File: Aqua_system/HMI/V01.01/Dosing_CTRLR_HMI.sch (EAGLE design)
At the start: 62 parts, among them IC1 74LS47N, Q1 BC817, Q2 BC817, Q3 BC817, Q4 BC817, X1 MICROMATCH-16

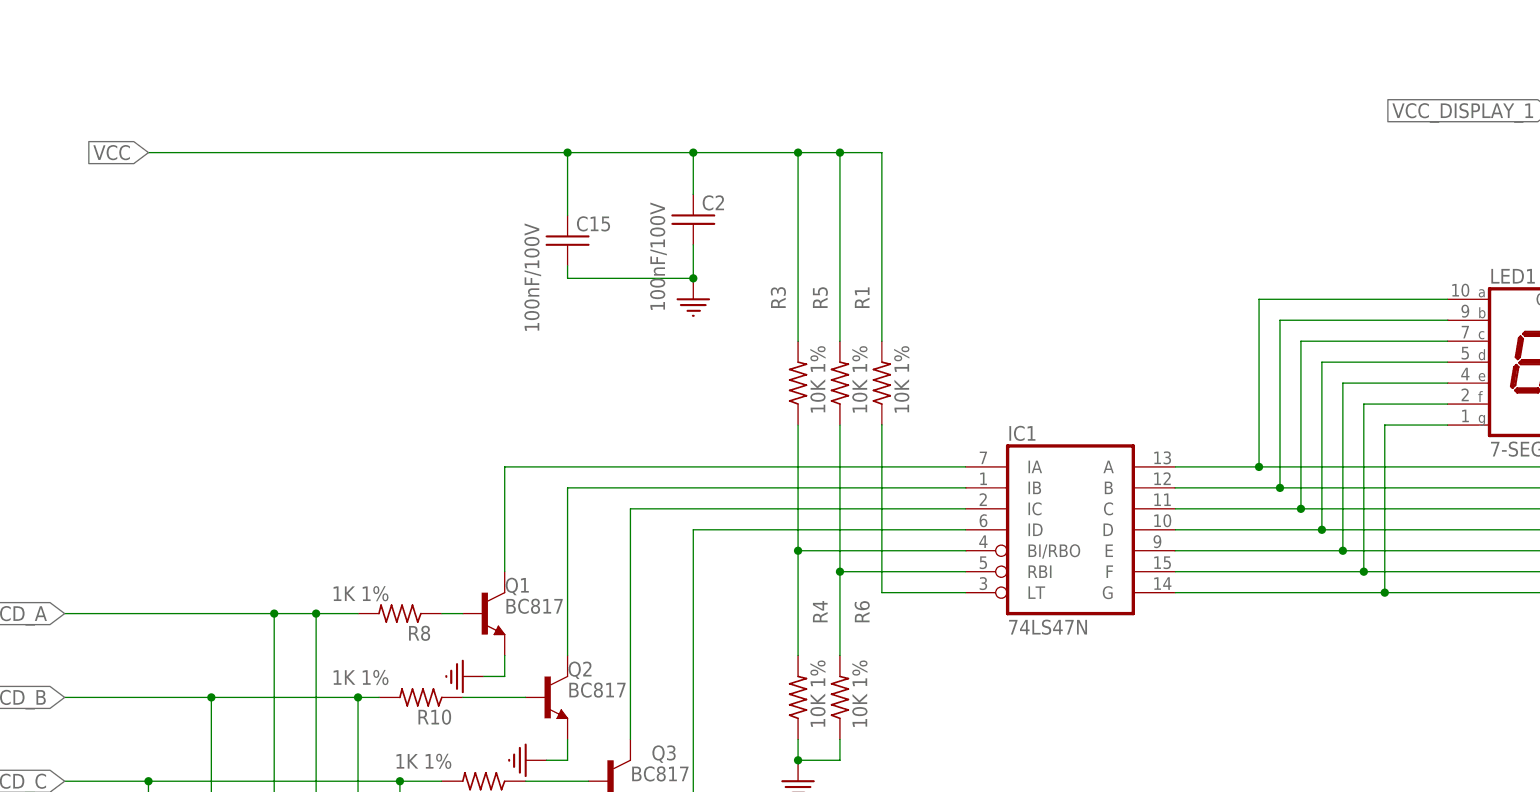
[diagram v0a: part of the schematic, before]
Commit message: Dosing Controller HMI HW01.01
Minor Changes introduced.
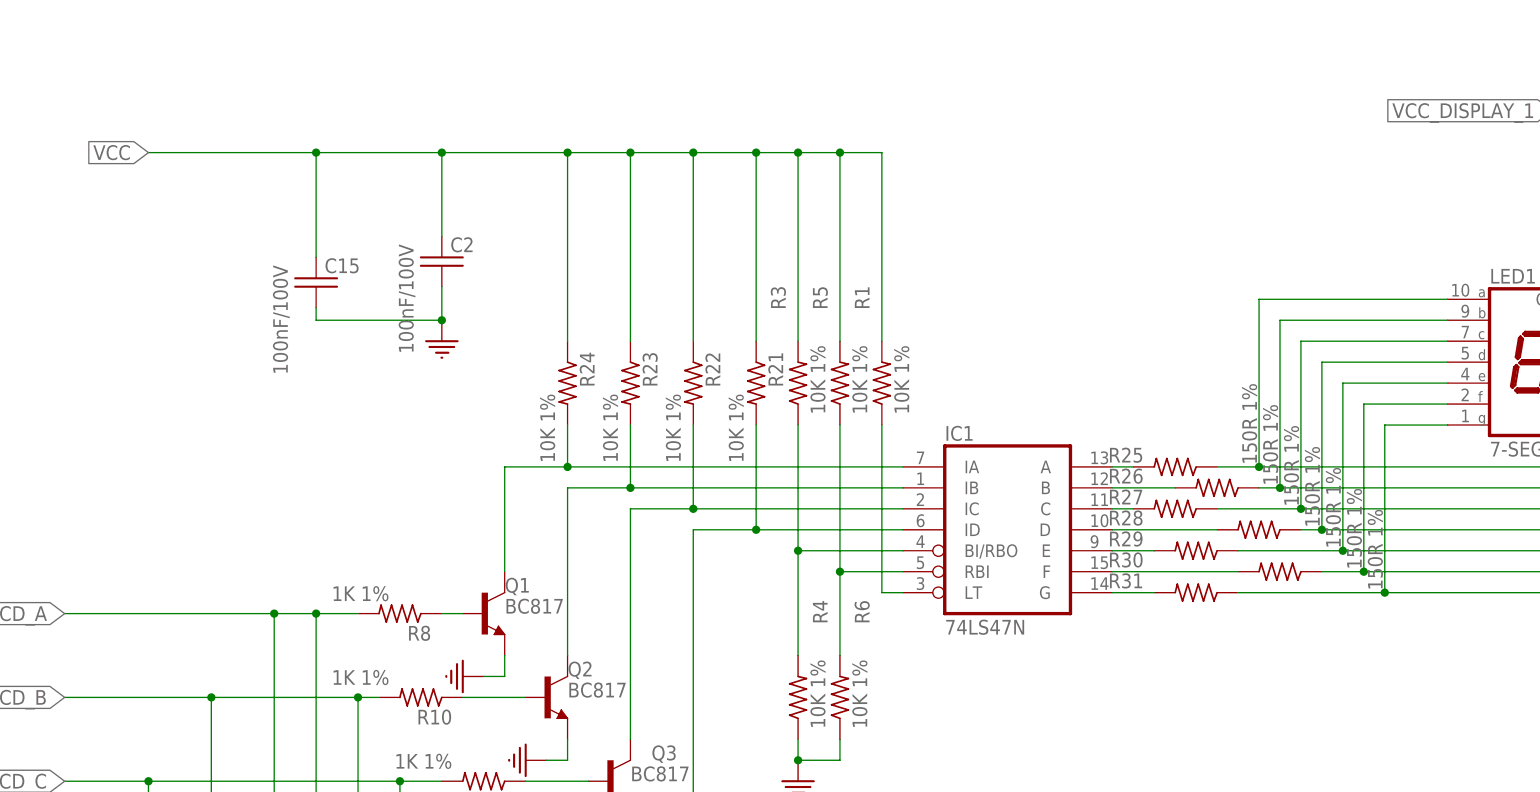
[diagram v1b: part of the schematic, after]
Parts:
- added R21, R22, R23, R24: 10K 1%, Labops_Lib_AH:R_0603
- added R25, R26, R27, R28, R29, R30, R31: 150R 1%, Labops_Lib_AH:R_1206EIA1206
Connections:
- new net N$12: IC1G$1.A, R25.2
- new net N$27: IC1G$1.B, R26.2
- new net N$28: IC1G$1.C, R27.2
- new net N$29: IC1G$1.D, R28.2
- new net N$30: IC1G$1.E, R29.2
- new net N$31: IC1G$1.F, R30.2
- new net N$32: IC1G$1.G, R31.2
- net N$1: now also R25.1; no longer IC1G$1.A
- net N$19: now also R24.2
- net N$2: now also R26.1; no longer IC1G$1.B
- net N$20: now also R23.2
- net N$21: now also R22.2
- net N$22: now also R21.2
- net N$3: now also R27.1; no longer IC1G$1.C
- net N$4: now also R28.1; no longer IC1G$1.D
- net N$5: now also R29.1; no longer IC1G$1.E
- net N$6: now also R30.1; no longer IC1G$1.F
- net N$7: now also R31.1; no longer IC1G$1.G
- net VCC: now also R21.1, R22.1, R23.1, R24.1
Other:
- moved on the sheet: C15, C2, IC1

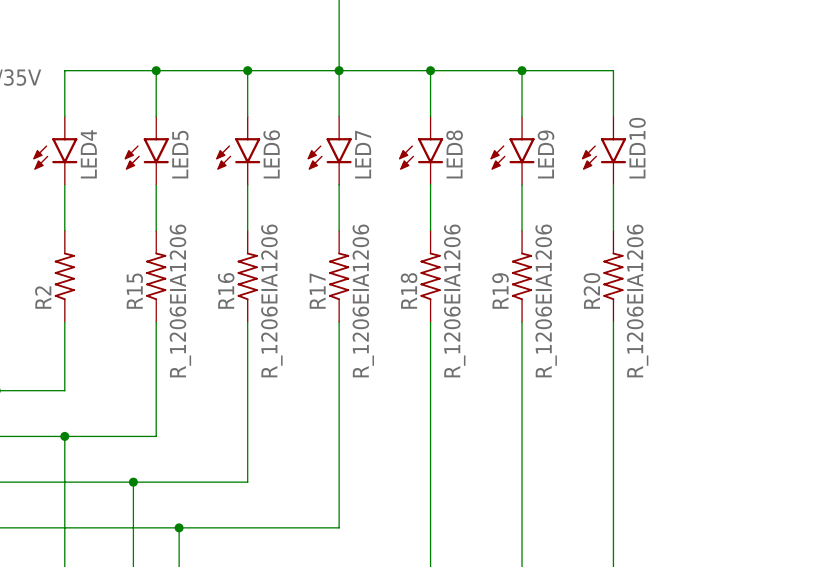
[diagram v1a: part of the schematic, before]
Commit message: HW02.02
Improvements after HW Functional Testing
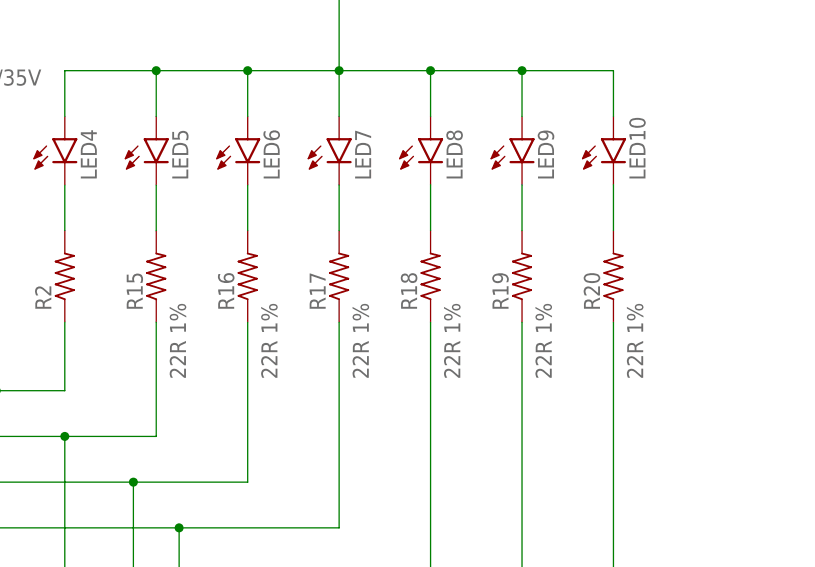
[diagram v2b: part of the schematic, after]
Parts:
- R15, R16, R17, R18, R19, R2, R20: value R_1206EIA1206 -> 22R 1%
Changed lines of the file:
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@@
 <part name="GND15" library="Labops_Lib_AH" deviceset="GND" device=""/>
 <part name="LED4" library="led" library_urn="urn:adsk.eagle:library:259" deviceset="LED" device="5MM" package3d_urn="urn:adsk.eagle:package:15799/2"/>
-<part name="R2" library="Labops_Lib_AH" deviceset="R_1206" device="EIA1206"/>
-<part name="R15" library="Labops_Lib_AH" deviceset="R_1206" device="EIA1206"/>
-<part name="R16" library="Labops_Lib_AH" deviceset="R_1206" device="EIA1206"/>
-<part name="R17" library="Labops_Lib_AH" deviceset="R_1206" device="EIA1206"/>
-<part name="R18" library="Labops_Lib_AH" deviceset="R_1206" device="EIA1206"/>
-<part name="R19" library="Labops_Lib_AH" deviceset="R_1206" device="EIA1206"/>
-<part name="R20" library="Labops_Lib_AH" deviceset="R_1206" device="EIA1206"/>
+<part name="R2" library="Labops_Lib_AH" deviceset="R_1206" device="EIA1206" value="22R 1%"/>
+<part name="R15" library="Labops_Lib_AH" deviceset="R_1206" device="EIA1206" value="22R 1%"/>
+<part name="R16" library="Labops_Lib_AH" deviceset="R_1206" device="EIA1206" value="22R 1%"/>
+<part name="R17" library="Labops_Lib_AH" deviceset="R_1206" device="EIA1206" value="22R 1%"/>
+<part name="R18" library="Labops_Lib_AH" deviceset="R_1206" device="EIA1206" value="22R 1%"/>
+<part name="R19" library="Labops_Lib_AH" deviceset="R_1206" device="EIA1206" value="22R 1%"/>
+<part name="R20" library="Labops_Lib_AH" deviceset="R_1206" device="EIA1206" value="22R 1%"/>
 <part name="LED5" library="led" library_urn="urn:adsk.eagle:library:259" deviceset="LED" device="5MM" package3d_urn="urn:adsk.eagle:package:15799/2"/>
 <part name="LED6" library="led" library_urn="urn:adsk.eagle:library:259" deviceset="LED" device="5MM" package3d_urn="urn:adsk.eagle:package:15799/2"/>
